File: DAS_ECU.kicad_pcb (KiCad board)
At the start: 2 copper layers, 156 x 85 mm, 144 parts, among them J1 Raspberry_Pi_2_3, J10 WHEEL_RIGHT, J11 BUZZER, J12 SD, J13 SPARE_PINS, J2 CAN, J3 POWER, J4 SWDEBUG_CONN, J5 BRAKELIGHT, J6 PEDAL_BOX, J7 BRAKE_REAR, J8 STEERING_WHEEL, J9 WHEEL_LEFT, K1 EX12U1S, Q1 2N7002NXAKR, Q2 2N7002NXAKR, Q3 2N7002NXAKR, Q4 2N7002NXAKR, Q5 2N7002NXAKR, SW1 RESET, U1 Tex_DCDC_v2, U10 MCP2562-E-SN, U11 MCP2562-E-SN, U12 STM32F446RETx, U13 M95256-WMN6P, U14 BMI088, U2 LD1117S50TR_SOT223, U3 MAX490E, U4 LM358PWR, U5 MP3V5004DP, U6 LM358PWR, U7 MCP2562-E-SN, U8 UA9637A, U9 UA9637A, Y1 ECS-160-18-33 16Mhz

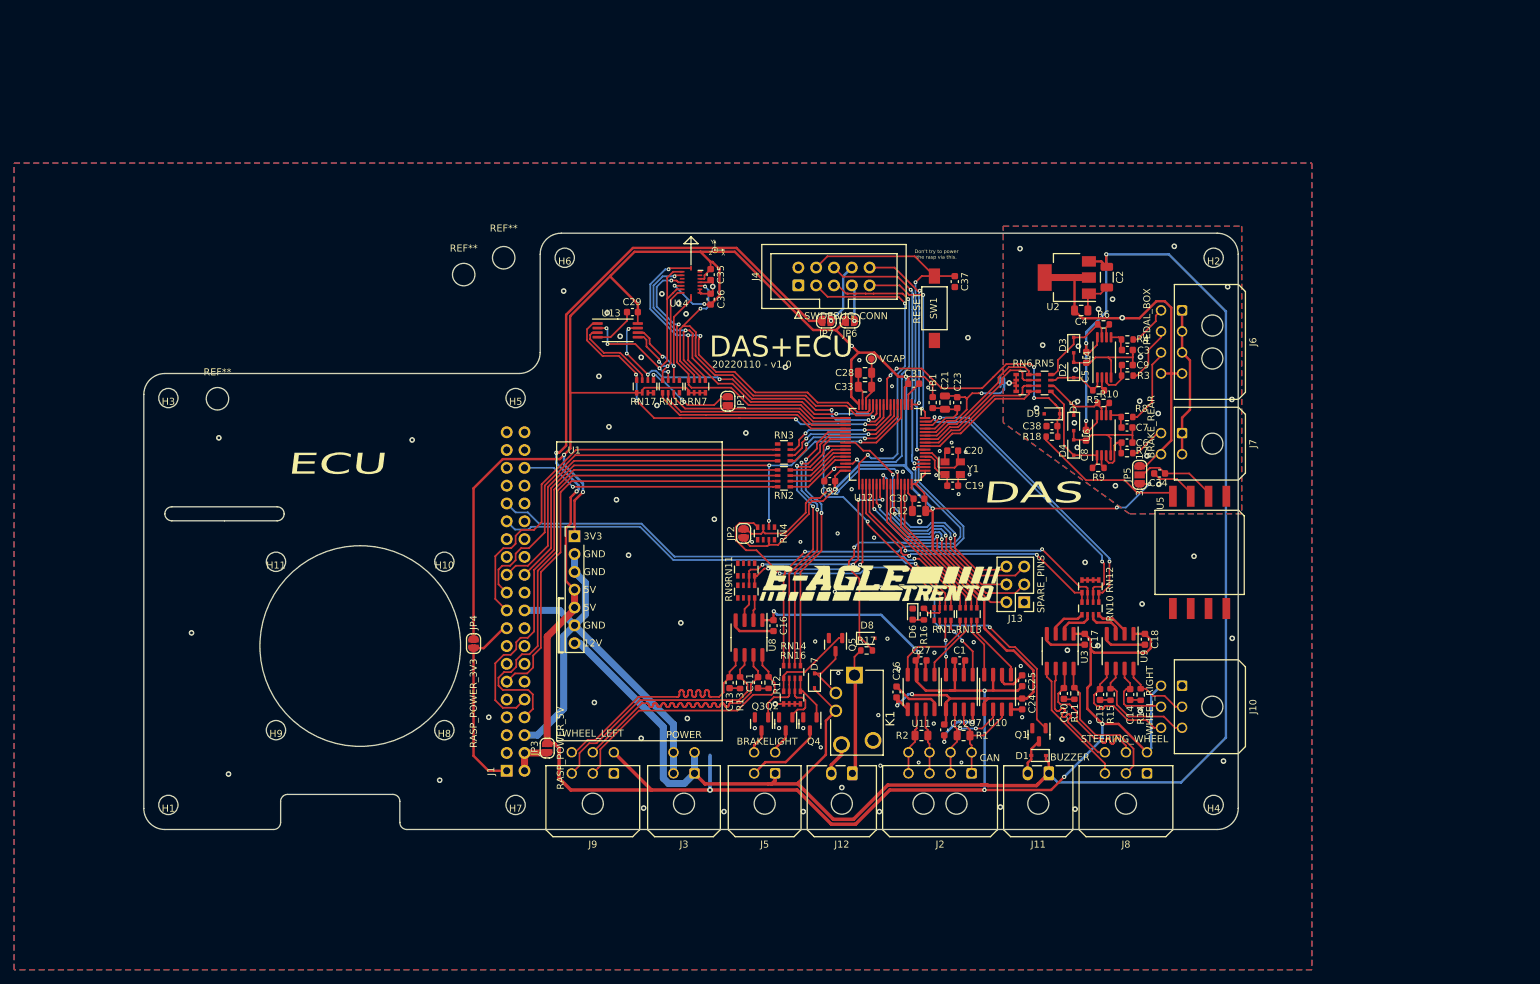
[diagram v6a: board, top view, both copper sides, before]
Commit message: added MCP2515
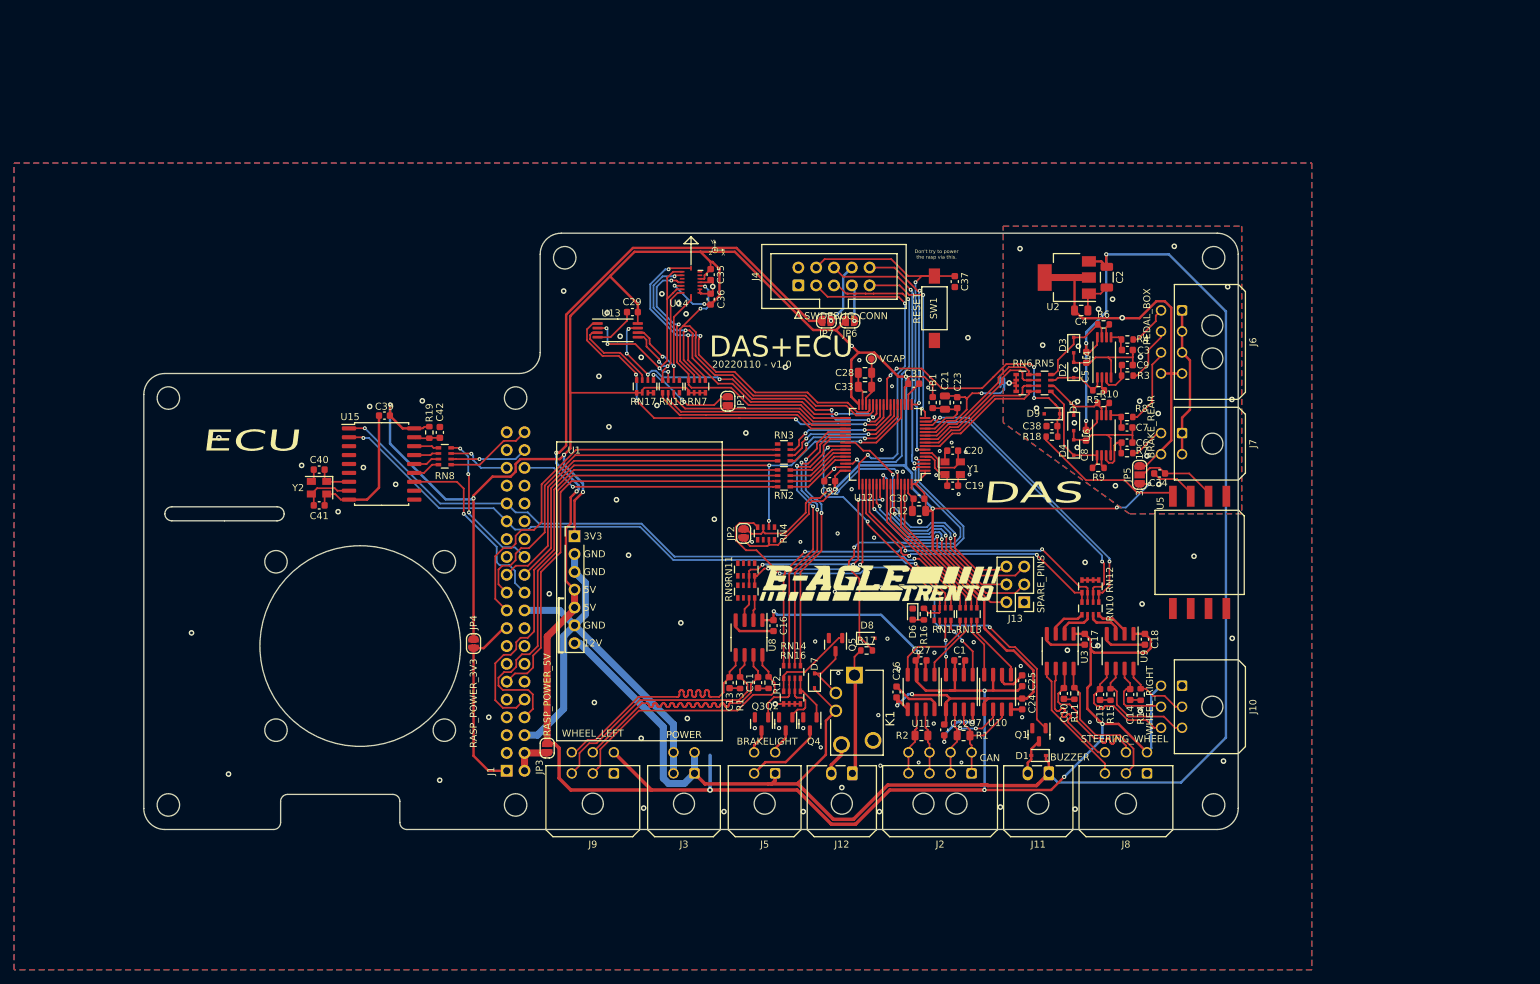
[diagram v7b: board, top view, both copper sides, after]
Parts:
- removed REF**: MountingHole_3.2mm_M3_ISO14580, MountingHole:MountingHole_3.2mm_M3_ISO14580
- removed REF**: MountingHole_3.2mm_M3_DIN965, MountingHole:MountingHole_3.2mm_M3_DIN965
- removed REF**: MountingHole_3.2mm_M3, MountingHole:MountingHole_3.2mm_M3
- added C39: 100nF, Capacitor_SMD:C_0603_1608Metric, F.Cu at (119.8, 77.0)
- added C40: 20pF, Capacitor_SMD:C_0603_1608Metric, F.Cu at (110.5, 84.7)
- added C41: 20pF, Capacitor_SMD:C_0603_1608Metric, F.Cu at (110.5, 89.8)
- added C42: 100nF, Capacitor_SMD:C_0603_1608Metric, F.Cu at (127.7, 79.4)
- added R19: 100k, Resistor_SMD:R_0603_1608Metric, F.Cu at (126.2, 79.4)
- added RN8: 33, Resistor_SMD:R_Array_Convex_4x0603, F.Cu at (128.4, 82.8)
- added U15: MCP2515-xSO, Package_SO:SOIC-18W_7.5x11.6mm_P1.27mm, F.Cu at (119.4, 83.9)
- added Y2: ECS-160-18-33 16Mhz, Crystal:Crystal_SMD_EuroQuartz_MT-4Pin_3.2x2.5mm, F.Cu at (110.5, 87.3)
- H1, H10, H11, H2, H3, H4, H5, H6, H7, H8, H9: footprint Eagle_Main:MountingHole_2.75_6.1Free -> Eagle_Main:MountingHole_3.2mm_M3_ISO14580
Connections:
- J1 pad 22: Net-(J1-Pad22) -> /Brain_Rasp/~INT~
- J1 pad 26: Net-(J1-Pad26) -> /Brain_Rasp/RASP_CAN_CS
- J1 pad 35: Net-(J1-Pad35) -> /Brain_Rasp/RASP_SPI1_MISO
- J1 pad 38: Net-(J1-Pad38) -> /Brain_Rasp/RASP_SPI1_MOSI
- J1 pad 40: Net-(J1-Pad40) -> /Brain_Rasp/RASP_SPI1_CLK
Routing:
- net +3V3: track 359.0 -> 388.0 mm, vias 12 -> 14
- net /Brain_Rasp/CANRX_NVIDIA: track 69.1 -> 96.6 mm, vias 1 -> 2
- net /Brain_Rasp/CANTX_NVIDIA: track 71.1 -> 98.0 mm, vias 1 -> 2
- net /Brain_Rasp/~INT~: track 0.00 -> 26.7 mm, vias 0 -> 1
- net GND: track 152.8 -> 175.1 mm, vias 84 -> 90
- net /Brain_Rasp/RASP_CAN_CS: track 0.00 -> 21.6 mm, vias 0 -> 3
- net /Brain_Rasp/RASP_SPI1_CLK: track 0.00 -> 12.4 mm
- net /Brain_Rasp/RASP_SPI1_MOSI: track 0.00 -> 11.0 mm, vias 0 -> 1
- net /Brain_Rasp/RASP_SPI1_MISO: track 0.00 -> 9.15 mm, vias 0 -> 1
- net Net-(C41-Pad1): track 0.00 -> 7.62 mm
- net Net-(C40-Pad1): track 0.00 -> 5.00 mm
- net /Brain_Rasp/RASP_SPI1_CLK_1: track 0.00 -> 3.93 mm
- net /Brain_Rasp/RASP_SPI1_MOSI_1: track 0.00 -> 3.74 mm
- net Net-(C42-Pad2): track 0.00 -> 3.73 mm
- net /Brain_Rasp/RASP_CAN_CS_1: track 0.00 -> 3.55 mm
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
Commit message: removed kicad v5 files
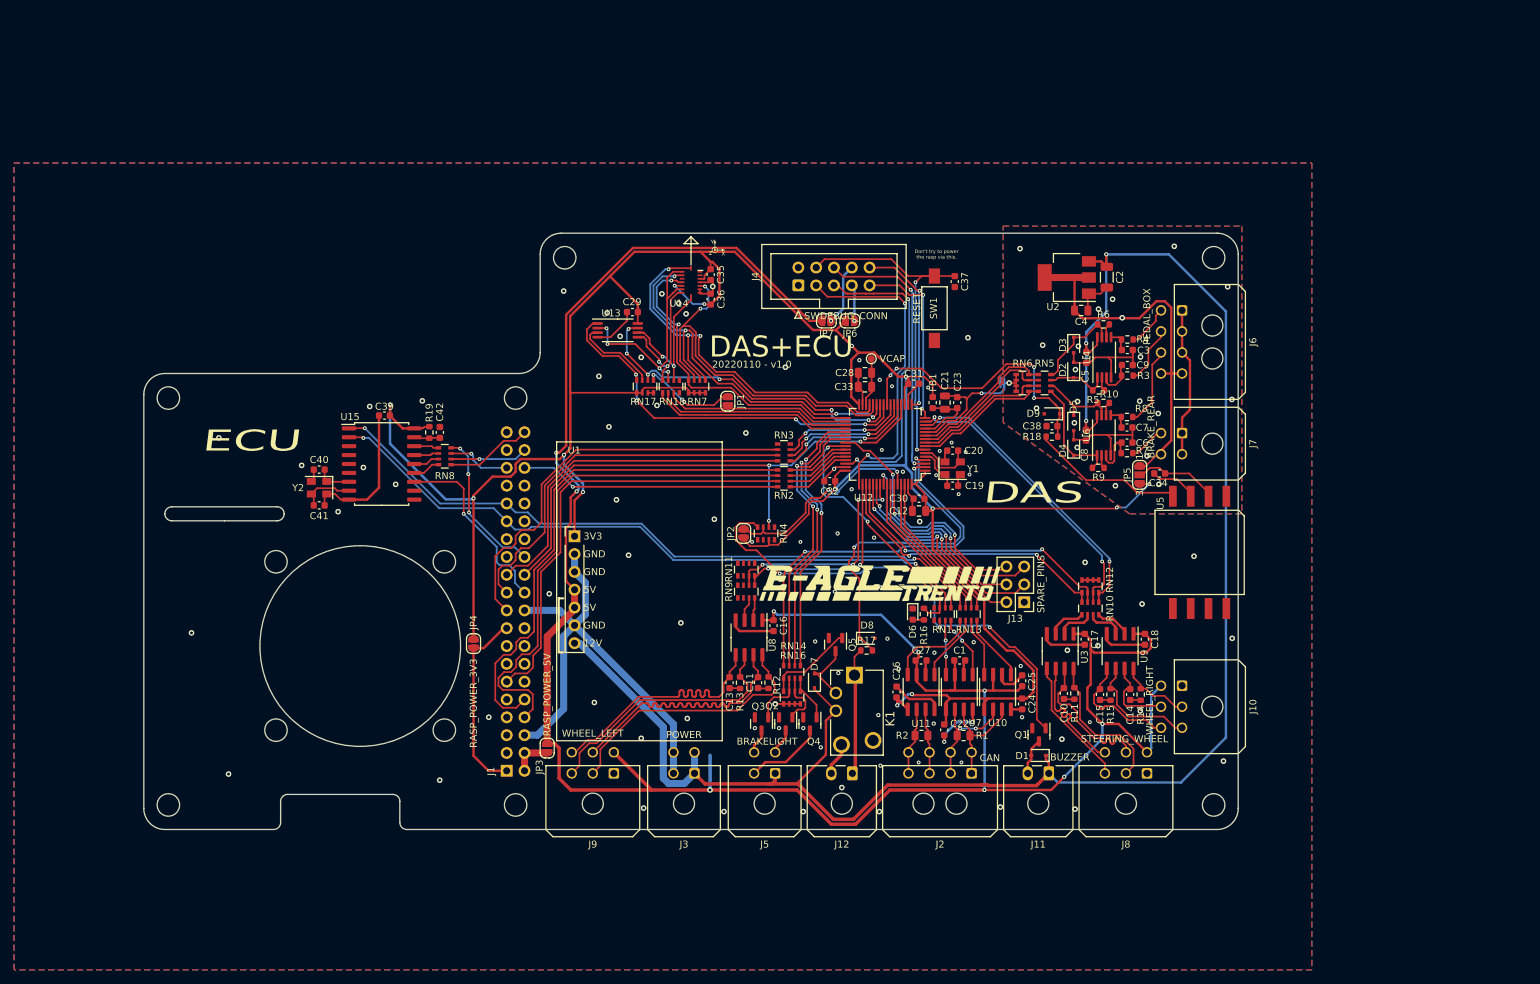
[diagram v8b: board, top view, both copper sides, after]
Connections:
- net /Brain_Rasp/~CS_EEPROM~ renamed /Brain_Rasp/~{CS_EEPROM}
- net /Brain_Rasp/~HOLD~ renamed /Brain_Rasp/~{HOLD}
- net /Brain_Rasp/~INT~ renamed /Brain_Rasp/~{INT}
- net /Brain_Rasp/~W~ renamed /Brain_Rasp/~{W}
- net /~RST~ renamed /~{RST}
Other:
- net class Default removed
- net class SDC removed
